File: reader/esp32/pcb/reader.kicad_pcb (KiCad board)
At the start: 2 copper layers, 104.9 x 38.4 mm, 12 parts, among them U2 RDM6300, U3 ESP32mini

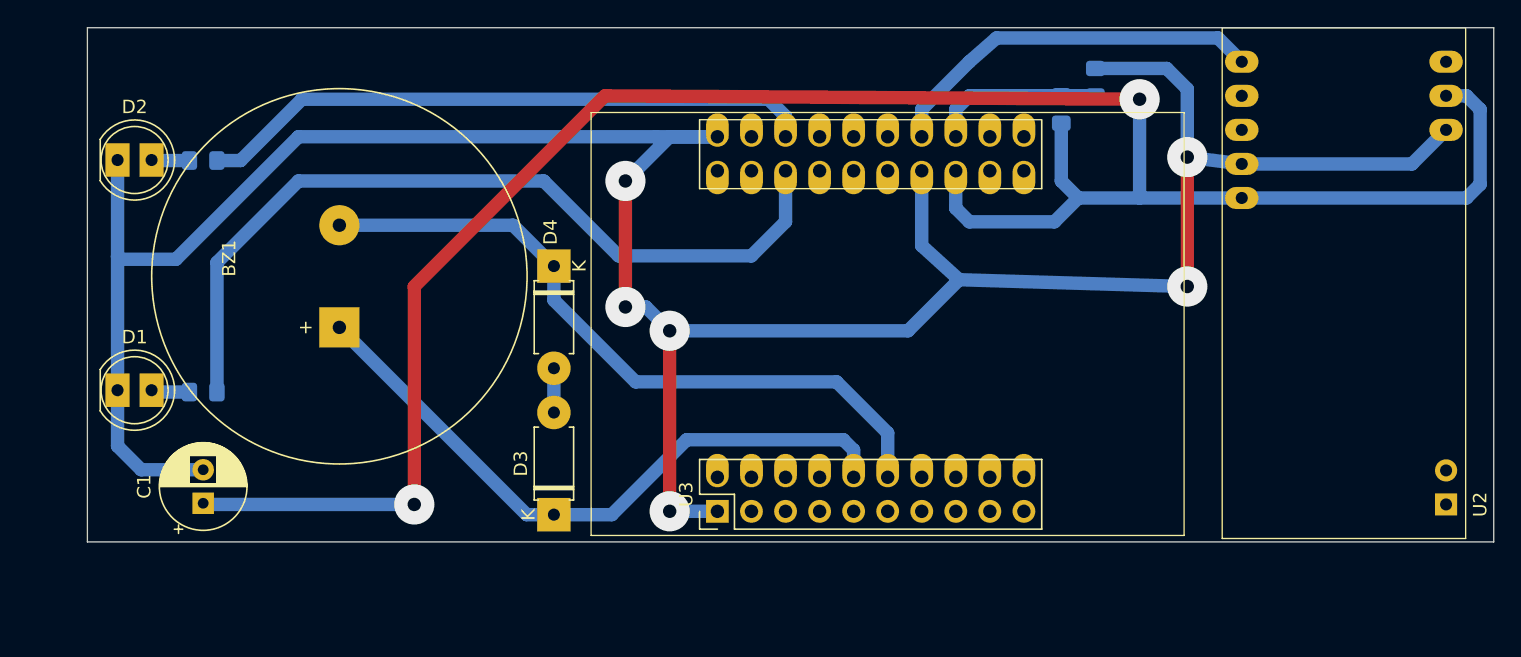
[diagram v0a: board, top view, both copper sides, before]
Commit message: Fix footprints.
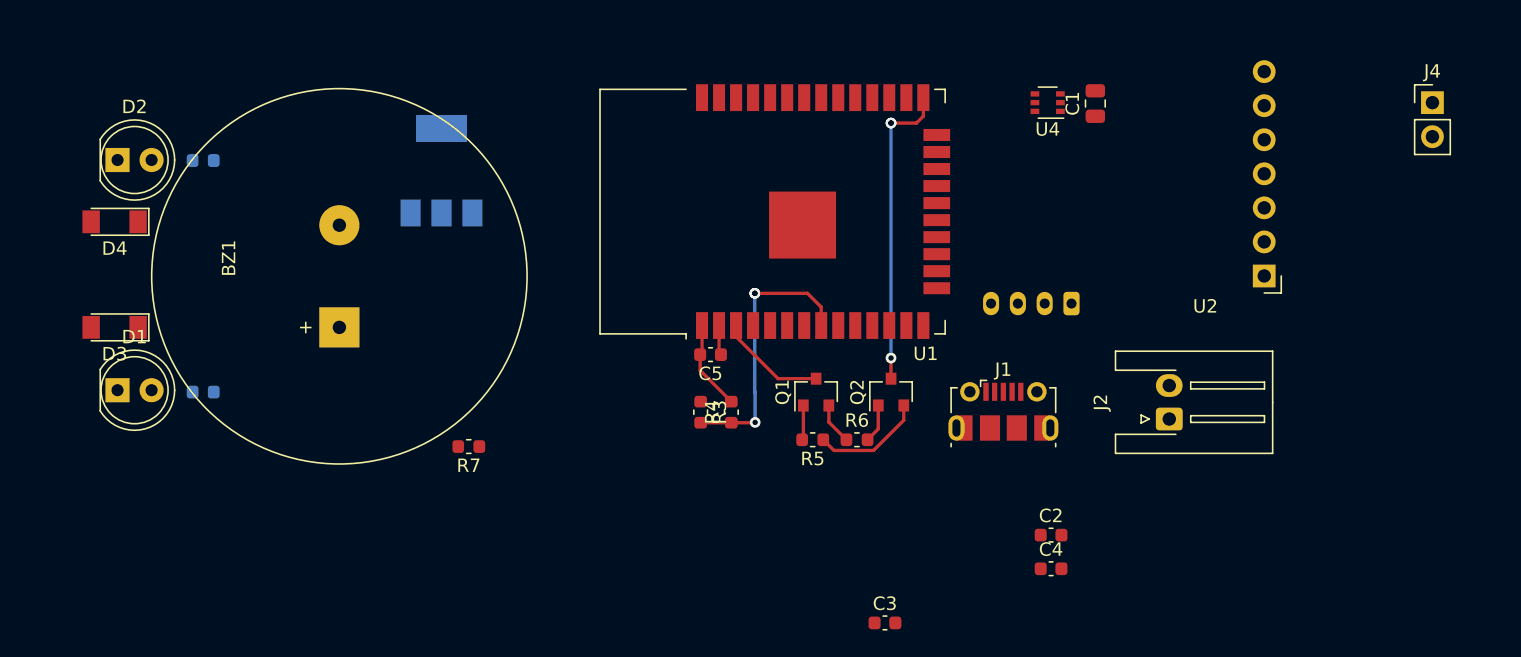
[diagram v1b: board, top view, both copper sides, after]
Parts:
- removed U3: ESP32mini, Module:ESP32mini
- added C2: C, Capacitor_SMD:C_0603_1608Metric, F.Cu at (119.6, 78.0)
- added C3: C, Capacitor_SMD:C_0603_1608Metric, F.Cu at (107.2, 84.5)
- added C4: 100n, Capacitor_SMD:C_0603_1608Metric, F.Cu at (119.6, 80.5)
- added C5: 100n, Capacitor_SMD:C_0603_1608Metric, F.Cu at (94.2, 64.5)
- added J1: Conn_01x06, Connector_USB:USB_Micro-B_Molex-105017-0001, F.Cu at (116.1, 68.8)
- added J2: Conn_01x02, Connector_JST:JST_XH_S02B-XH-A-1_1x02_P2.50mm_Horizontal, F.Cu at (128.5, 69.3)
- added J3: Conn_01x04, Connector_JST:JST_PH_B4B-PH-K_1x04_P2.00mm_Vertical, B.Cu at (121.2, 60.7)
- added J4: Conn_01x02, Connector_PinHeader_2.54mm:PinHeader_1x02_P2.54mm_Vertical, F.Cu at (148.1, 45.7)
- added Q1: MMBT3904, Package_TO_SOT_SMD:SOT-23, F.Cu at (102.1, 67.3)
- added Q2: MMBT3904, Package_TO_SOT_SMD:SOT-23, F.Cu at (107.7, 67.3)
- added R5: 10K, Resistor_SMD:R_0603_1608Metric, F.Cu at (101.9, 70.9)
- added R6: 10K, Resistor_SMD:R_0603_1608Metric, F.Cu at (105.2, 70.9)
- added R7: 100, Resistor_SMD:R_0603_1608Metric, F.Cu at (76.2, 71.4)
- added U1: ESP32-WROOM-32U, RF_Module:ESP32-WROOM-32, F.Cu at (101.9, 53.8)
- added U4: 74LVC1T45, Package_TO_SOT_SMD:SOT-363_SC-70-6, F.Cu at (119.4, 45.7)
- added U5: AMS1117-3.3, Package_TO_SOT_SMD:SOT-223-3_TabPin2, B.Cu at (74.2, 50.8)
- C1: value 100u -> 10u; footprint Capacitor_THT:CP_Radial_D6.3mm_P2.50mm -> Capacitor_SMD:C_0805_2012Metric
- D3, D4: footprint Diode_THT:D_A-405_P7.62mm_Horizontal -> Diode_SMD:D_MiniMELF
- R1, R2: footprint Resistor_SMD:R_0805_2012Metric_Pad1.15x1.40mm_HandSolder -> Resistor_SMD:R_0603_1608Metric
- R3, R4: footprint Resistor_SMD:R_0805_2012Metric_Pad1.15x1.40mm_HandSolder -> Resistor_SMD:R_0603_1608Metric; moved to F.Cu
- U2: value RDM6300 -> RF125-PS; footprint Module:RDM6300_B38.5x18.2mm -> Module:rf125ps
- moved C1 72.9 mm to (122.9, 45.8)
- moved R4 36.6 mm to (95.8, 68.8)
- moved D3 35.6 mm to (49.8, 62.5), turned to 180 degrees
- moved R3 35.1 mm to (93.5, 68.8), turned to -90 degrees
- moved D4 32.9 mm to (49.8, 54.6), turned to 180 degrees
- moved U2 21.8 mm to (135.5, 58.6), turned to 180 degrees
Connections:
- net BUZ1 renamed Net-(BZ1-Pad1)
- net Net-(R3-Pad2) renamed SENSE
- U2 pad 1: unconnected-(U2-Pad1) -> GND
- U2 pad 2: unconnected-(U2-Pad2) -> +5V
- U2 pad 3: GND -> Net-(U2-Pad3)
- U2 pad 4: +5V -> unconnected-(U2-Pad4)
- U2 pad 6: RFID_TX -> Net-(J4-Pad2)
- U2 pad 7: unconnected-(U2-Pad7) -> Net-(J4-Pad1)
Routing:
- net GND: track 207.9 -> 6.69 mm, vias 6 -> 0
- net +5V: track 157.5 -> 0.00 mm, vias 2 -> 0
- net RED: track 61.8 -> 0.00 mm
- net BUZ2: track 52.1 -> 0.00 mm
- net Net-(BZ1-Pad1): track 48.8 -> 0.00 mm
- net GREEN: track 46.4 -> 0.00 mm
- net RFID_TX: track 28.8 -> 0.00 mm
- net IO0: track 0.00 -> 23.1 mm, vias 0 -> 3
- net Net-(Q2-Pad2): track 0.00 -> 8.37 mm
- net EN: track 0.00 -> 8.10 mm
- net SENSE: track 12.9 -> 20.5 mm, vias 0 -> 3
- net Net-(D3-Pad2): track 3.30 -> 0.00 mm
- net Net-(Q1-Pad2): track 0.00 -> 3.10 mm
- net Net-(Q2-Pad1): track 0.00 -> 2.89 mm
- net Net-(D1-Pad2): track 2.88 -> 0.00 mm
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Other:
- board outline removed

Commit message: Finish routing.
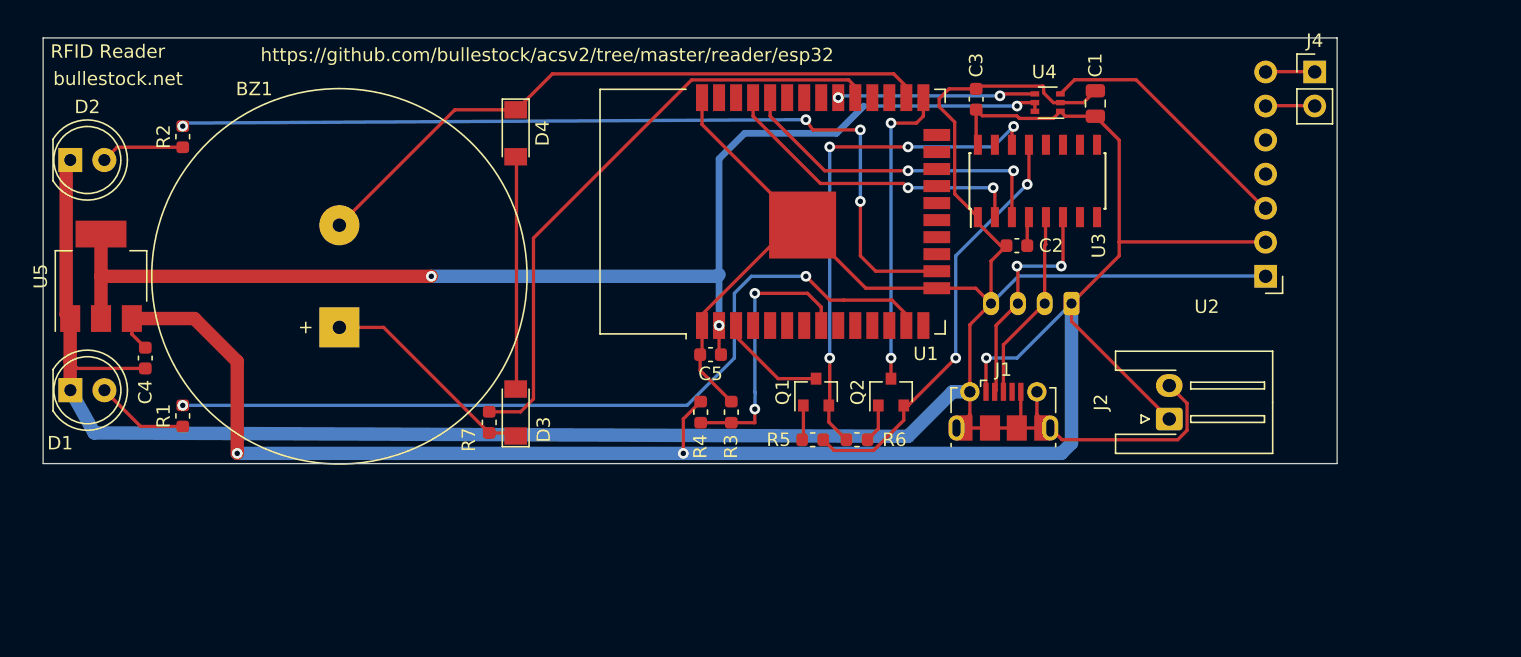
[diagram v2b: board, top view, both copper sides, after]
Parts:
- added U3: CH340C, Housings_SOIC:SOIC-16_3.9x9.9mm_Pitch1.27mm, F.Cu at (118.6, 51.6)
- R1, R2, U5: moved to F.Cu
- moved C4 69.4 mm to (52.1, 64.8), turned to -90 degrees
- moved C3 39.6 mm to (114.0, 45.5), turned to 90 degrees
- moved D4 30.6 mm to (79.7, 48.0), turned to -90 degrees
- moved D3 30.6 mm to (79.7, 68.8), turned to 90 degrees
- moved U5 26.6 mm to (48.8, 58.7)
- moved C2 21.7 mm to (117.1, 56.4), turned to 180 degrees
- moved J4 9.08 mm to (139.3, 43.4)
- moved D2 3.52 mm to (46.5, 50.0)
- moved D1 3.52 mm to (46.5, 67.2)
- moved R7 2.36 mm to (77.7, 69.6), turned to -90 degrees
- moved R2 2.34 mm to (54.9, 48.3), turned to 90 degrees
- moved R1 2.34 mm to (54.9, 69.1), turned to 90 degrees
- moved U2 0.11 mm to (135.6, 58.7)
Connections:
- U1 pad 13: GREEN -> RED
- U1 pad 16: RED -> GREEN
- U1 pad 26: BUZ1 -> BUZ2
- U1 pad 29: BUZ2 -> BUZ1
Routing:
- net GND: track 6.69 -> 229.8 mm
- net +5V: track 0.00 -> 157.4 mm, vias 0 -> 3
- net +3V3: track 2.23 -> 93.1 mm, vias 0 -> 3
- net GREEN: track 0.00 -> 66.6 mm, vias 0 -> 4
- net RED: track 0.00 -> 62.8 mm, vias 0 -> 2
- net BUZ2: track 0.00 -> 48.2 mm
- net BUZ1: track 0.00 -> 45.6 mm
- net Net-(Q1-Pad2): track 3.10 -> 38.2 mm, vias 0 -> 4
- net RX: track 0.00 -> 24.7 mm, vias 0 -> 2
- net TX: track 0.00 -> 23.7 mm, vias 0 -> 2
- net Net-(Q2-Pad2): track 8.37 -> 31.9 mm, vias 0 -> 2
- net Net-(U2-Pad3): track 0.00 -> 19.6 mm
- net Net-(D3-Pad2): track 0.00 -> 17.3 mm
- net Net-(J1-Pad2): track 0.00 -> 17.1 mm, vias 0 -> 2
- net Net-(BZ1-Pad1): track 0.00 -> 16.6 mm
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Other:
- board outline added: 96.5 x 31.8 mm
- board text added: "RFID Reader"
- board text added: "bullestock.net"
- board text added: "https://github.com/bullestock/acsv2/tree/master/reader/esp32"

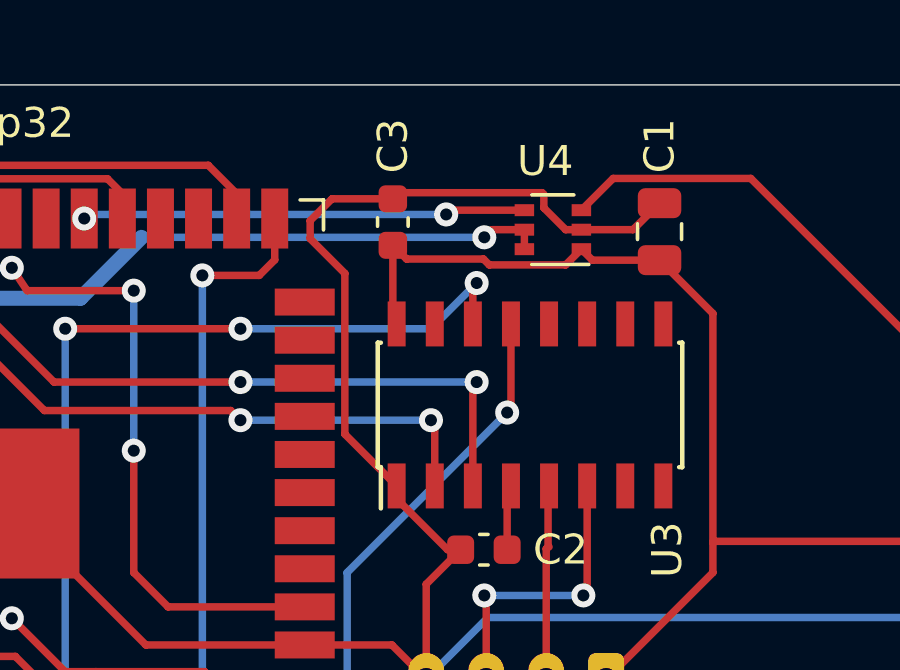
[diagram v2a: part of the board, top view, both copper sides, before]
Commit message: Fix footprint for 74LVC1T45.
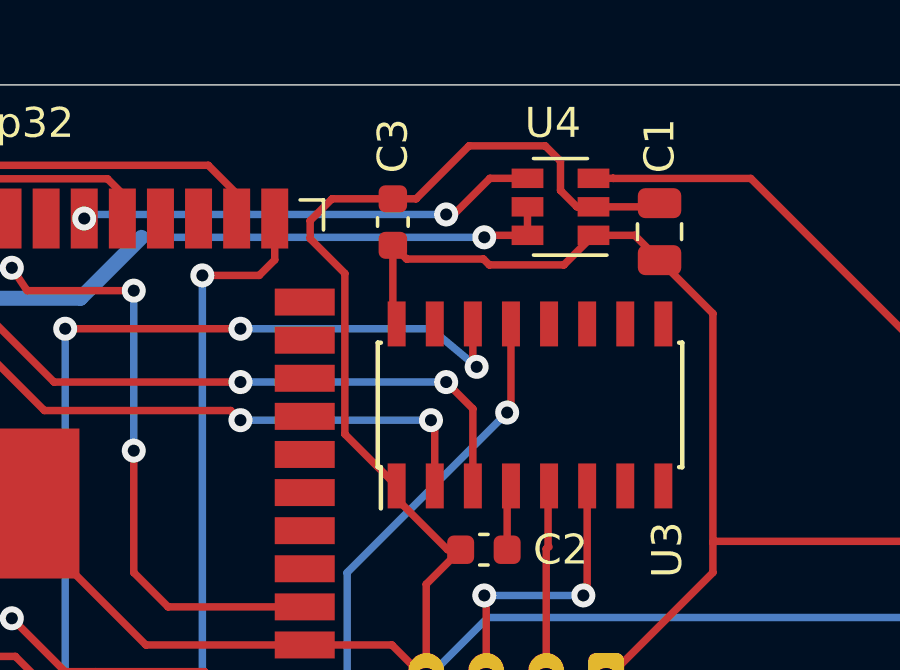
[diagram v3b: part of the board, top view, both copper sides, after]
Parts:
- U4: footprint Package_TO_SOT_SMD:SOT-363_SC-70-6 -> Package_TO_SOT_SMD:SOT-23-6
- moved U4 0.80 mm to (119.6, 45.0)
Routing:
- net GND: track 229.8 -> 231.1 mm
- net Net-(U2-Pad3): track 19.6 -> 18.8 mm
- net ESP_RFID_TX: track 14.8 -> 15.5 mm
- net RX: track 24.7 -> 24.0 mm

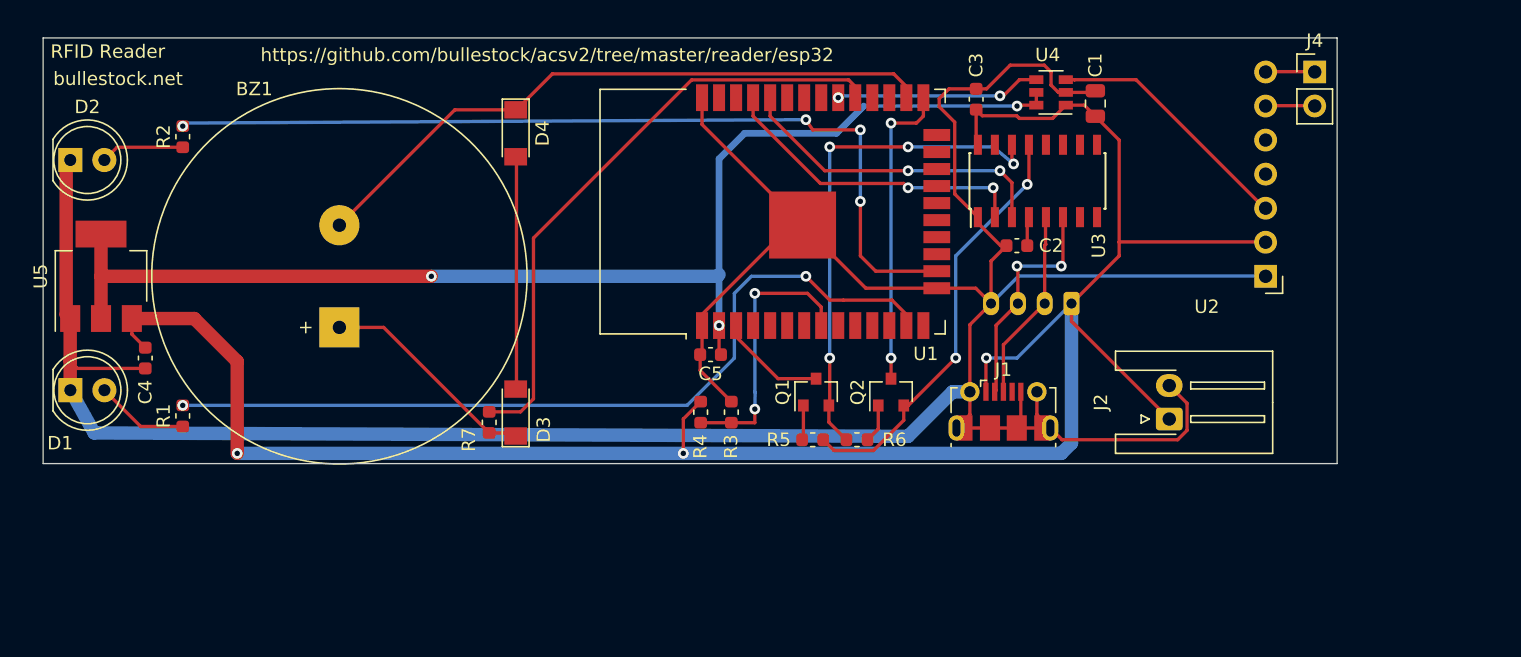
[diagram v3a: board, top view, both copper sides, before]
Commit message: Fix switched RX/TX, adjust dimensions.
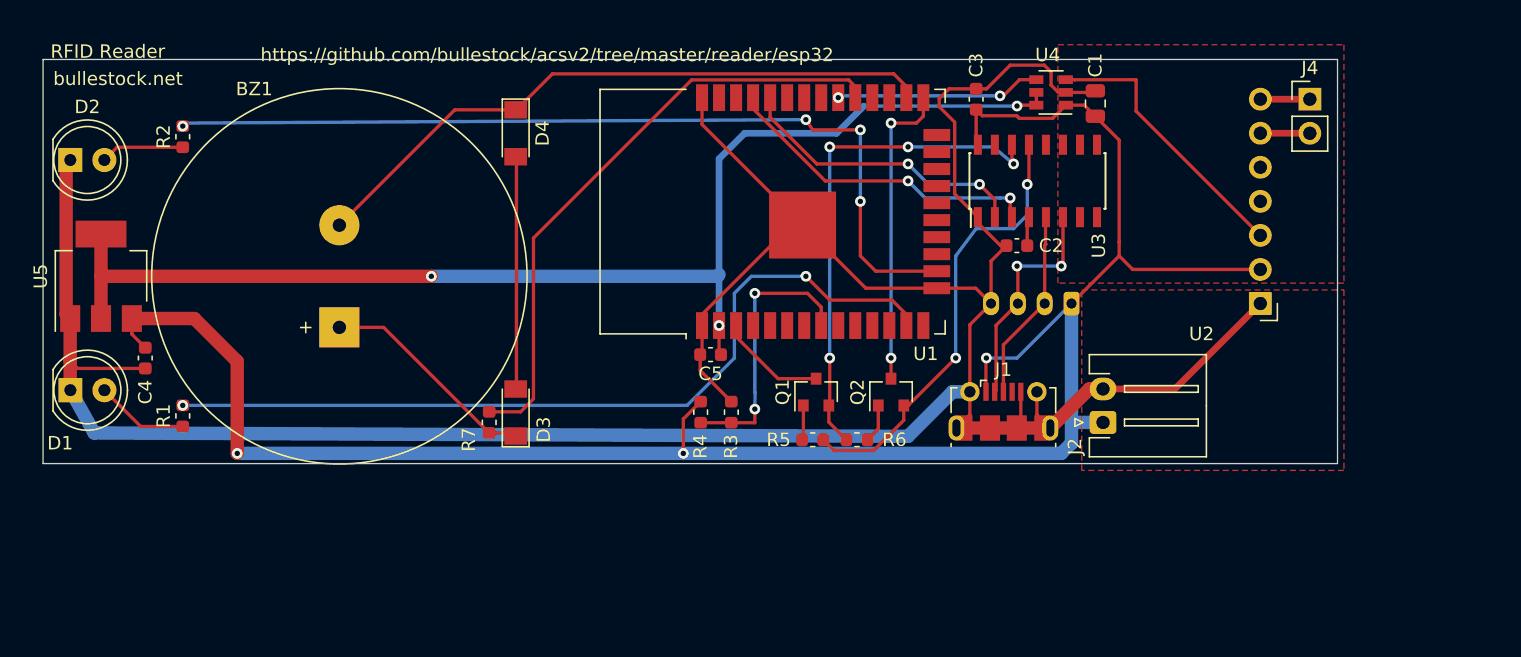
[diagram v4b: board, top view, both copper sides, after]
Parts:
- moved J2 4.95 mm to (123.5, 69.6)
- moved J4 2.07 mm to (138.9, 45.5)
- moved U2 2.07 mm to (135.2, 60.7)
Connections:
- U1 pad 34: RX -> ESP_RX
- U1 pad 35: TX -> ESP_TX
- U3 pad 10: unconnected-(U3-Pad10) -> (no net)
- U3 pad 11: unconnected-(U3-Pad11) -> (no net)
- U3 pad 12: unconnected-(U3-Pad12) -> (no net)
- U3 pad 15: unconnected-(U3-Pad15) -> (no net)
- U3 pad 2: TX -> ESP_RX
- U3 pad 3: RX -> ESP_TX
- U3 pad 7: unconnected-(U3-Pad7) -> (no net)
- U3 pad 8: unconnected-(U3-Pad8) -> (no net)
- U3 pad 9: unconnected-(U3-Pad9) -> (no net)
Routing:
- net ESP_TX: track 0.00 -> 24.2 mm, vias 0 -> 2
- net RX: track 24.0 -> 0.00 mm, vias 2 -> 0
- net TX: track 23.7 -> 0.00 mm, vias 2 -> 0
- net ESP_RX: track 0.00 -> 22.1 mm, vias 0 -> 2
- net GND: track 231.1 -> 221.6 mm
- net +5V: track 157.8 -> 148.7 mm
- net Net-(U2-Pad3): track 18.8 -> 20.7 mm
- net Net-(Q2-Pad2): track 31.9 -> 33.4 mm
- added copper zone on F.Cu, net +5V
- added copper zone on F.Cu, net GND
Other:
- board size 96.5 x 31.8 mm -> 96.5 x 30.1 mm

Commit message: Fix switched D-/D+.
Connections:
- J1 pad 3: Net-(J1-Pad3) -> Net-(J3-Pad3)
- J3 pad 2: Net-(J1-Pad3) -> Net-(J1-Pad2)
- J3 pad 3: Net-(J1-Pad2) -> Net-(J3-Pad3)
- U3 pad 5: Net-(J1-Pad3) -> Net-(J3-Pad3)
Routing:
- net Net-(J3-Pad3): track 0.00 -> 14.4 mm, vias 0 -> 1
- net Net-(J1-Pad3): track 14.4 -> 0.00 mm
- net Net-(J1-Pad2): track 17.1 -> 18.2 mm, vias 2 -> 0

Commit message: Cleanup.
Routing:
- net GND: track 221.6 -> 211.4 mm
- net ESP_TX: track 24.2 -> 23.2 mm
- net RED: track 62.8 -> 62.0 mm
- net EN: track 8.10 -> 7.27 mm
- net BUZ2: track 48.2 -> 47.4 mm
- net BUZ1: track 45.6 -> 44.8 mm
